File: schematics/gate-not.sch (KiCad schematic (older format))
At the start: 3 parts, among them Q13 NPN

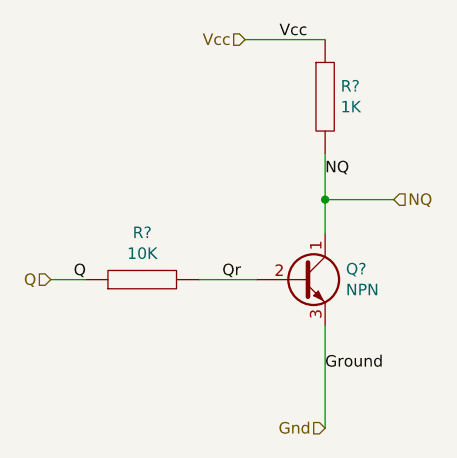
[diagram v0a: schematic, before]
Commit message: Adds a test for the 4-4-1 multiplexer
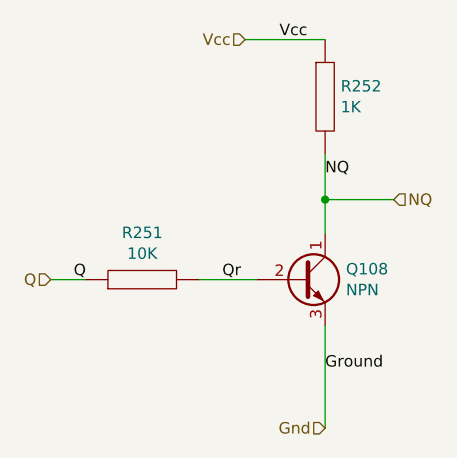
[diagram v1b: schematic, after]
